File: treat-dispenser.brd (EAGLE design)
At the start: 33 x 47 mm, 40 parts, among them U1 MCP73831, U2 TPS61032, U3 ATMEGA32U4, Y1 16MHz

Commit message: added part numbers for bom, manufacturing files
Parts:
- removed L1: 6.8uH, SparkFun-Passives:0603
- added L2: (no value), SparkFun-Passives:INDUCTOR-SRP4020
- JP1: value WM17115-ND -> (none)
- JP3, JP4: value SJ1-3523N -> (none)
- JP6: value FEMALE 2x3 -> (none)
- R10, R8: value 1.62M -> 1M
- R11: value 180K -> 110K
- R3: value 300K -> 182K
- U2: value TPS61032 -> TPS6103x
- moved JP8 6.62 mm to (26.2, 35.1)
- moved JP5 6.61 mm to (28.7, 35.1)
- moved JP7 2.96 mm to (28.7, 23.9)
- moved JP2 2.54 mm to (23.4, 40.9)
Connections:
- net SW: now also L2.P$2; no longer L1.2
- net V_BATT: now also L2.P$1; no longer L1.1
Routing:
- net V_BATT: track 37.2 -> 42.6 mm
- net A0: track 13.2 -> 8.40 mm
- net A1: track 34.4 -> 38.8 mm
- net D5: track 16.8 -> 13.2 mm
- net SW: track 3.60 -> 6.30 mm
- net VCC: track 100.8 -> 98.3 mm
- net N$8: track 3.08 -> 4.40 mm
- net D13: track 5.21 -> 4.64 mm
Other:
- board text added: "in"
- board text added: "out"
- board text removed: "sen"
- board text removed: "servo"
- board text removed: "srv"

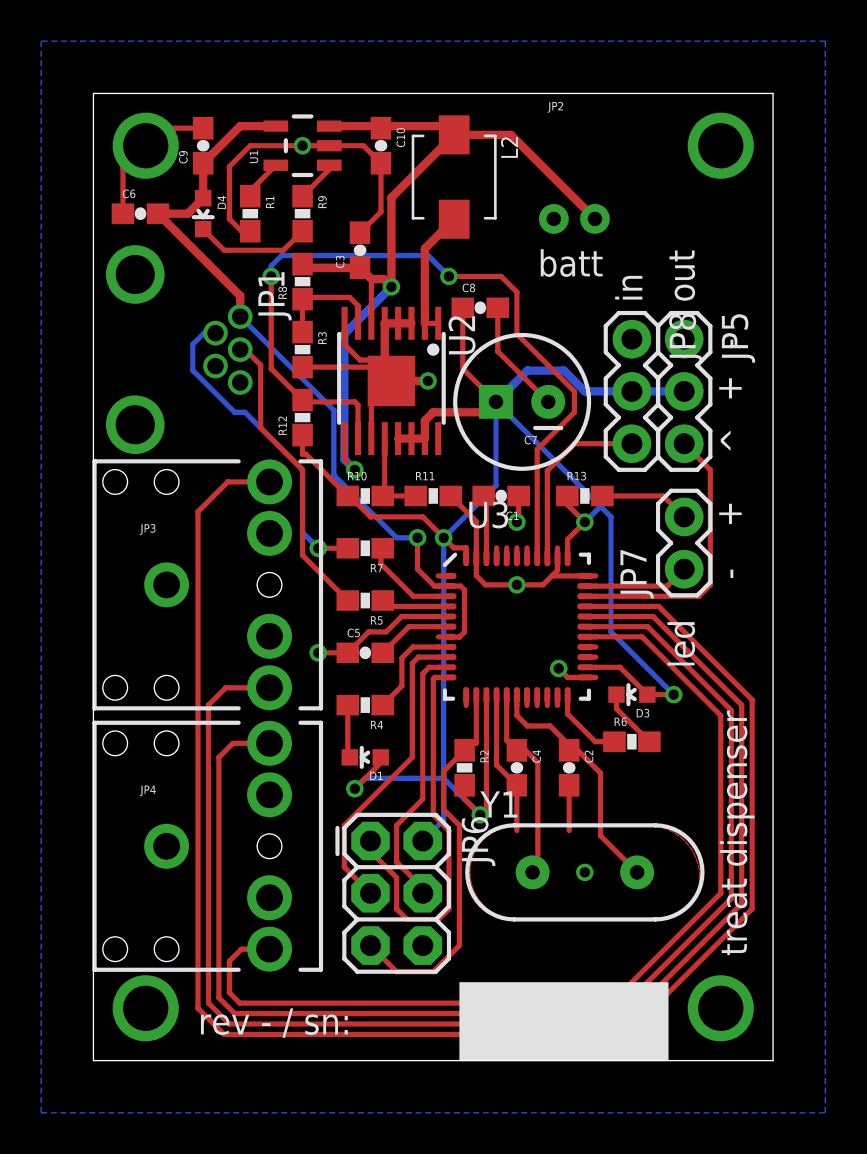
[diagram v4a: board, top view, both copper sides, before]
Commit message: fixed part names
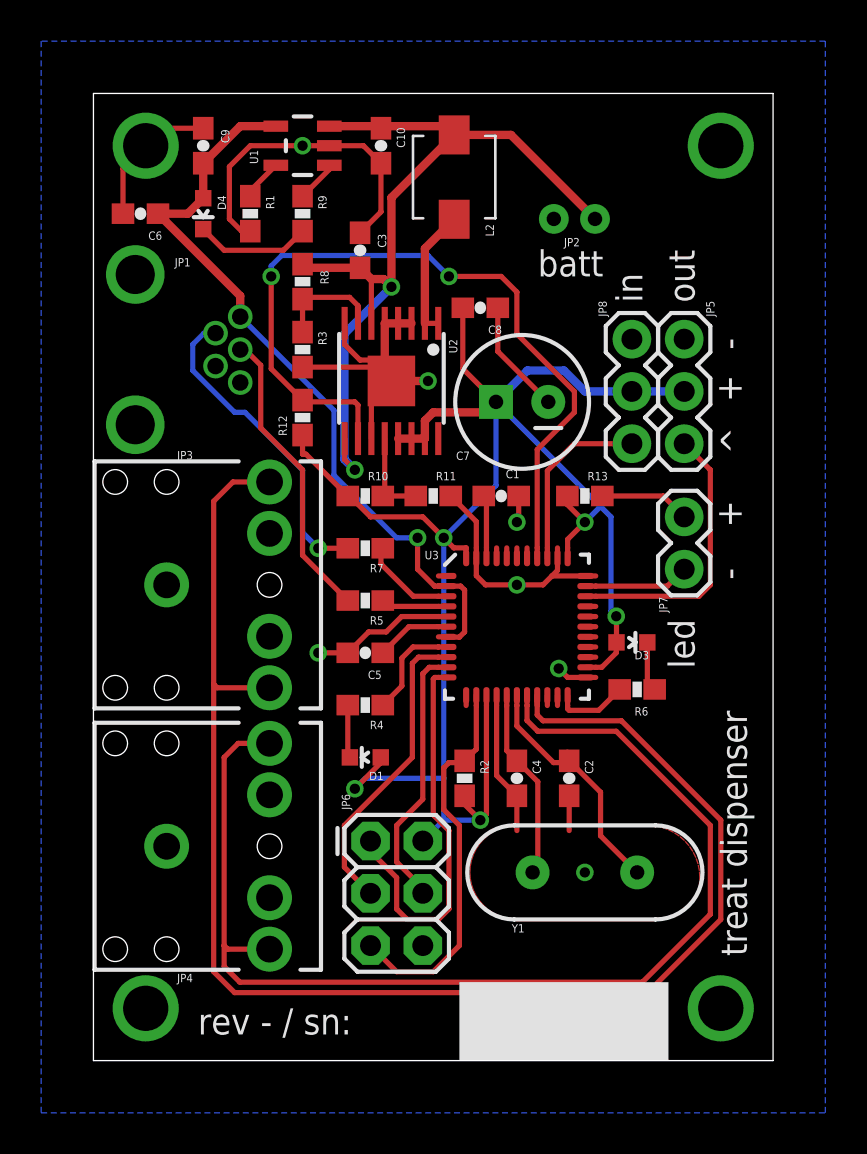
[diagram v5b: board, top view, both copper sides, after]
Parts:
- moved R6 2.55 mm to (26.4, 18.0)
- moved D3 2.54 mm to (26.2, 20.3), turned to 270 degrees
- moved C2 0.51 mm to (23.1, 13.7)
- moved C4 0.51 mm to (20.6, 13.7)
- moved R2 0.51 mm to (18.0, 13.7)
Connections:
- net D10: no longer JP3.RING
- net D2: now also JP3.RING, JP3.TIP
- net D3: now also JP4.RING, JP4.TIP
- net D6: no longer JP4.TIP
- net D8: no longer JP4.RING
- net D9: no longer JP3.TIP
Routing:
- net D10: track 77.8 -> 0.00 mm
- net D2: track 0.00 -> 72.1 mm
- net D9: track 65.1 -> 0.00 mm
- net D8: track 59.4 -> 0.00 mm
- net D3: track 0.00 -> 56.3 mm
- net D6: track 46.3 -> 0.00 mm
- net VCC: track 98.3 -> 91.3 mm
- net RESET: track 17.5 -> 18.4 mm
- net N$7: track 2.95 -> 2.43 mm
- net GND: track 74.7 -> 74.2 mm

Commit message: rev A initial commit
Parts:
- removed D1: Yellow, SparkFun:LED-0603
- removed D3: Green, SparkFun:LED-0603
- removed D4: red, SparkFun:LED-0603
- removed FRAME1: FRAME-LETTER, SparkFun-Aesthetics:CREATIVE_COMMONS
- removed JP4: (no value), SparkFun-Connectors:AUDIO-JACK
- removed JP8: (no value), SparkFun-Connectors:1X03
- removed R4, R6, R9: 470, SparkFun:0603-RES
- removed U3: ATMEGA32U4, Testing:QFN-44-NOPAD_1:1-OUTFAKES
- added U$1: ATMEGA32U4TQFP-44, SparkFun-DigitalIC:TQFP44
- moved JP1 99.5 mm to (99.1, 12.7), turned to 180 degrees
- moved JP3 94.6 mm to (97.8, 31.8), turned to 180 degrees
- moved C6 91.3 mm to (90.2, 16.5), turned to 180 degrees
- moved JP6 78.7 mm to (91.4, 21.0), turned to 0 degrees
- moved R7 78.6 mm to (90.2, 8.89), turned to 0 degrees
- moved R5 77.7 mm to (90.2, 11.4), turned to 0 degrees
- moved C5 77.2 mm to (90.2, 14.0), turned to 180 degrees
- moved R2 71.0 mm to (88.3, 24.1)
- moved Y1 67.2 mm to (87.1, 31.8), turned to 90 degrees
- moved C4 64.7 mm to (83.2, 29.8), turned to 90 degrees
- moved C2 63.3 mm to (83.2, 33.7)
- moved C1 54.6 mm to (72.4, 12.7)
- moved C9 35.6 mm to (3.81, 8.89), turned to 180 degrees
- moved U1 32.4 mm to (3.81, 12.7), turned to 180 degrees
- moved R1 32.3 mm to (7.62, 8.89), turned to 0 degrees
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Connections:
- removed net N$5: D1.C, R4.2
- removed net N$7: D3.C, R6.2
- removed net STAT: R9.1, U1.1
- removed net TXLED: R6.1, U3.22
- net A0: now also U$1.36; no longer JP8.3, U3.36
- net A1: now also U$1.37; no longer U3.37
- net A2: now also U$1.38; no longer U3.38
- net A3: now also U$1.39; no longer U3.39
- net A4: now also U$1.40; no longer U3.40
- net A5: now also U$1.41; no longer U3.41
- net AREF: now also U$1.42; no longer U3.42
- net D10: now also U$1.30; no longer U3.30
- net D11: now also U$1.12; no longer U3.12
- net D12: now also U$1.26; no longer U3.26
- net D13: now also U$1.32; no longer U3.32
- net D14: now also U$1.8; no longer R4.1, U3.8
- net D2: now also U$1.19; no longer JP3.RING, U3.19
- net D3: now also JP3.RING, U$1.18; no longer JP4.RING, JP4.TIP, U3.18
- net D4: now also U$1.25, U1.1; no longer U3.25
- net D5: now also U$1.31; no longer U3.31
- net D6: now also U$1.27; no longer U3.27
- net D7: now also U$1.1; no longer U3.1
- net D8: now also U$1.28; no longer U3.28
- net D9: now also U$1.29; no longer U3.29
- net GND: now also U$1.15, U$1.23, U$1.33, U$1.35, U$1.43, U$1.5; no longer JP4.SLEEVE, JP8.1, U3.15, U3.23, U3.33, U3.35, U3.43, U3.5
- net MISO: now also U$1.11; no longer U3.11
- net MOSI: now also U$1.10; no longer U3.10
- net N$1: now also U$1.16; no longer U3.16
- net N$2: now also U$1.17; no longer U3.17
- net N$3: now also U$1.22; no longer D4.C, R9.2
- net N$4: now also U$1.6; no longer U3.6
- net RD+: now also U$1.4; no longer U3.4
- net RD-: now also U$1.3; no longer U3.3
- net RESET: now also U$1.13; no longer U3.13
- net RXI: now also U$1.20; no longer U3.20
- net SCK: now also U$1.9; no longer U3.9
- net TXO: now also U$1.21; no longer U3.21
- net UVCC: now also U$1.2, U$1.7; no longer D4.A, U3.2, U3.7
- net VCC: now also U$1.14, U$1.24, U$1.34, U$1.44; no longer D1.A, D3.A, JP8.2, U3.14, U3.24, U3.34, U3.44
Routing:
- net D4: track 0.00 -> 105.9 mm
- net D13: track 4.64 -> 64.7 mm
- net D5: track 13.2 -> 69.5 mm
- net D2: track 72.1 -> 23.1 mm
- net VCC: track 91.3 -> 125.4 mm, vias 5 -> 1
- net D3: track 56.3 -> 30.9 mm
- net A1: track 38.8 -> 55.9 mm, vias 2 -> 0
- net GND: track 74.2 -> 62.8 mm, vias 11 -> 12
- net D+: track 14.5 -> 3.47 mm
- net V_BATT: track 42.6 -> 53.6 mm, vias 2 -> 0
- net D-: track 15.5 -> 4.97 mm, vias 1 -> 0
- net MISO: track 18.6 -> 8.84 mm
- net RD+: track 2.82 -> 12.5 mm
- net RD-: track 4.24 -> 13.8 mm
- net UVCC: track 37.4 -> 46.0 mm, vias 1 -> 2
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- added copper zone on layer 16, net UVCC
- added copper zone on layer 16, net VCC
- removed copper zone on layer 1, net GND
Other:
- board size 33 x 47 mm -> 101.6 x 44.5 mm

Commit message: rev A update with new board dxf
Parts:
- added R4: 10K, SparkFun:0603-RES
- moved C1 12.7 mm to (59.7, 12.7)
- moved C2 12.7 mm to (70.5, 33.7)
- moved C4 12.7 mm to (70.5, 29.8)
- moved C5 12.7 mm to (77.5, 14.0)
- moved C6 12.7 mm to (77.5, 16.5)
- moved JP1 12.7 mm to (86.4, 12.7)
- moved JP3 12.7 mm to (85.1, 31.8)
- moved JP6 12.7 mm to (78.7, 21.0)
- moved R2 12.7 mm to (75.6, 24.1)
- moved R5 12.7 mm to (77.5, 11.4)
- moved R7 12.7 mm to (77.5, 8.89)
- moved U$1 12.7 mm to (63.5, 22.2)
- moved Y1 12.7 mm to (74.4, 31.8)
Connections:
- new net N$5: R4.2, U$1.33
- net GND: now also R4.1; no longer U$1.33
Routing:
- net D5: track 69.5 -> 56.8 mm
- net D13: track 64.7 -> 52.0 mm
- net A1: track 55.9 -> 43.2 mm
- net D4: track 105.9 -> 93.2 mm
- net UVCC: track 46.0 -> 50.2 mm
- net N$5: track 0.00 -> 2.57 mm
- net VCC: track 125.4 -> 128.0 mm
- net GND: track 62.8 -> 65.3 mm, vias 12 -> 11
- net D-: track 4.97 -> 6.24 mm
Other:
- board size 101.6 x 44.5 mm -> 88.9 x 44.5 mm
- board text added: "rev A / sn:"
- board text removed: "+"
- board text removed: "-"
- board text removed: "^"
- board text removed: "batt"
- board text removed: "in"
- board text removed: "led"
- board text removed: "out"
- board text removed: "rev - / sn:"
